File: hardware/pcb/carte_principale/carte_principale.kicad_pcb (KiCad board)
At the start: 2 copper layers, 54.5 x 50 mm, 20 parts, among them J1 Arduino_UNO_R3, J2 Conn_01x02, J3 Conn_01x02, P1 TE-FFC-10-0.5, P2 TE-FFC-10-0.5, U1 ESP-WROOM-02, U2 LSM6DS3, U3 BMP280, U4 74AHCT1G04, U5 74AHC1G125, U6 74LS166, U7 LIS2MDL

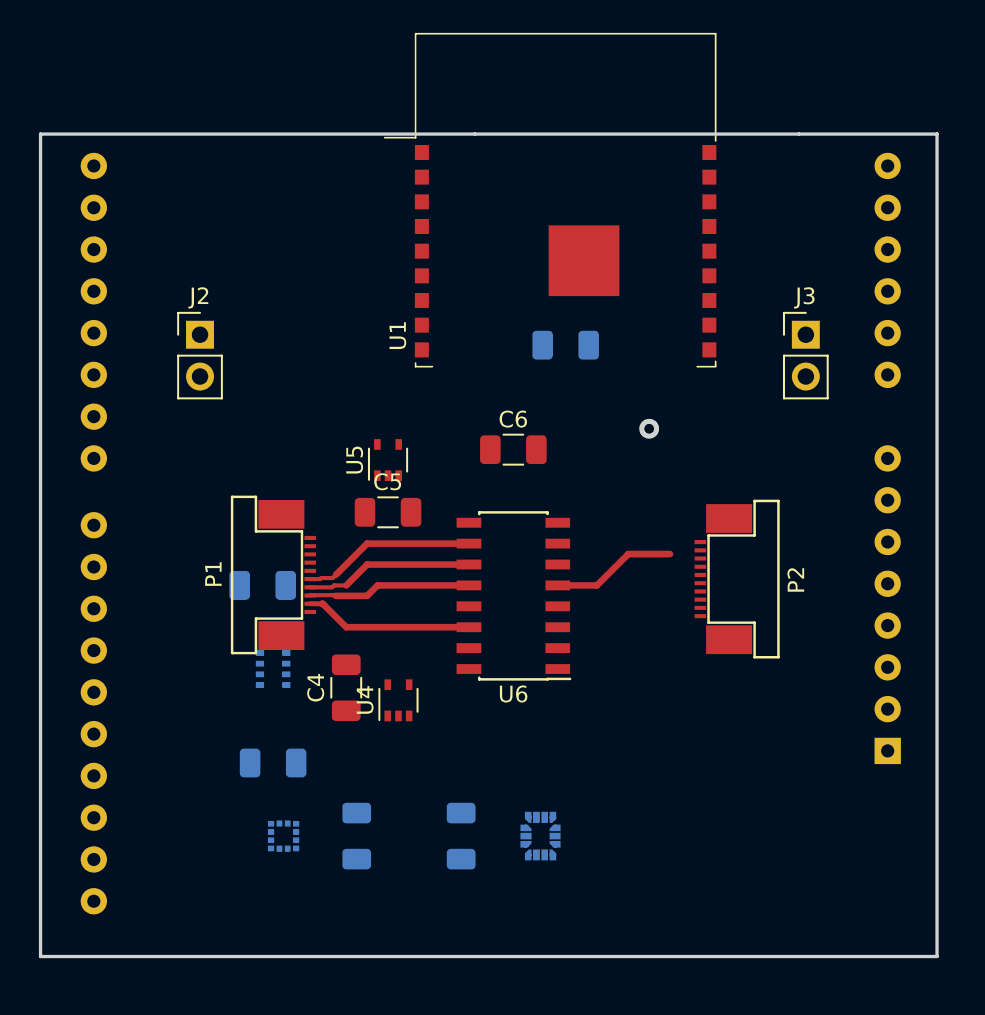
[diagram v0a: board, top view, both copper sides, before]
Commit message: ajout des pcb gauche et droit
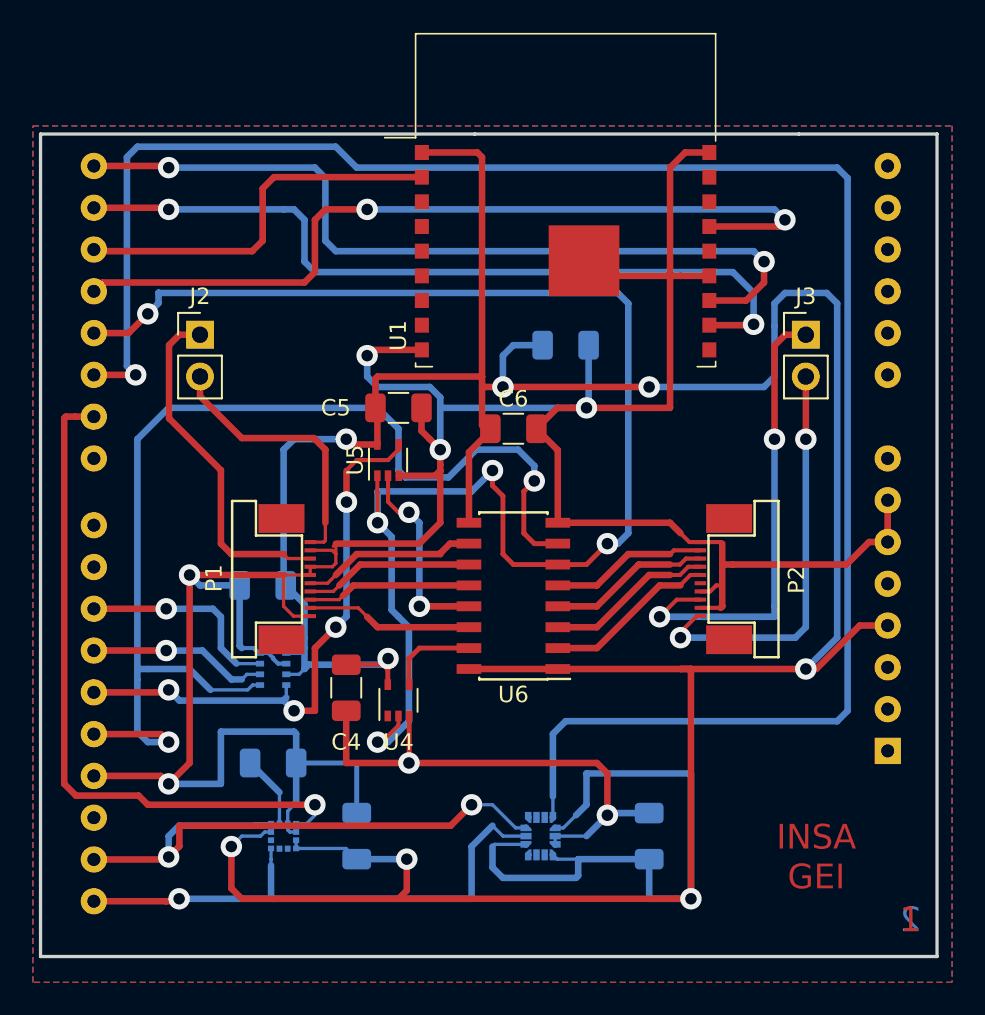
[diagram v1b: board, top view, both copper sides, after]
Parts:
- moved C2 11.4 mm to (127.0, 106.7)
- moved C5 6.38 mm to (111.8, 80.6)
- moved C6 1.27 mm to (118.7, 81.9)
- moved P1 0.25 mm to (106.0, 91.1)
- turned C4 to 270 degrees
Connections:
- C1 pad 1: VDD -> VCC
- C2 pad 1: VDD -> VCC
- C3 pad 1: VDD -> VCC
- C4 pad 1: VDD -> VCC
- C5 pad 1: VDD -> VCC
- C6 pad 1: VDD -> VCC
- C7 pad 1: VDD -> VCC
- J1 pad 4: VDD -> VCC
- U1 pad 1: VDD -> VCC
- U2 pad 12: VDD -> VCC
- U2 pad 5: VDD -> VCC
- U2 pad 8: VDD -> VCC
- U3 pad 6: VDD -> VCC
- U3 pad 8: VDD -> VCC
- U6 pad 1: VDD -> VCC
- U6 pad 16: VDD -> VCC
- U6 pad 9: VDD -> VCC
- U7 pad 10: VDD -> VCC
- U7 pad 3: VDD -> VCC
- U7 pad 9: VDD -> VCC
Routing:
- net VCC: track 0.00 -> 247.8 mm, vias 0 -> 8
- net GND: track 0.00 -> 217.6 mm, vias 0 -> 7
- net /IT_LSM6DS3: track 0.00 -> 116.8 mm, vias 0 -> 1
- net /KEYS_EN: track 0.00 -> 92.0 mm, vias 0 -> 5
- net /SPI_SCK: track 0.00 -> 68.8 mm, vias 0 -> 2
- net /WIFI_RST: track 0.00 -> 51.0 mm, vias 0 -> 2
- net /WIFI_TX: track 0.00 -> 50.4 mm, vias 0 -> 2
- net /WIFI_RX: track 0.00 -> 48.4 mm, vias 0 -> 2
- net /IT_LIS2MDL: track 0.00 -> 42.4 mm, vias 0 -> 1
- net /I2C_SDA: track 0.00 -> 36.8 mm, vias 0 -> 2
- net /SPI_MISO: track 0.00 -> 34.5 mm, vias 0 -> 4
- net /I2C_SCL: track 0.00 -> 33.4 mm, vias 0 -> 1
- net /Audio_Right_2: track 0.00 -> 28.6 mm, vias 0 -> 2
- net /Audio_Right_1: track 0.00 -> 25.1 mm, vias 0 -> 2
- net /WIFI_EN: track 0.00 -> 23.7 mm
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- added copper zone on B.Cu, net GND
- added copper zone on F.Cu, net GND
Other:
- board text added: "1"
- board text added: "2"
- board text added: "INSA GEI"

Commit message: ajout du wifi (debut) et mise a jour pcb
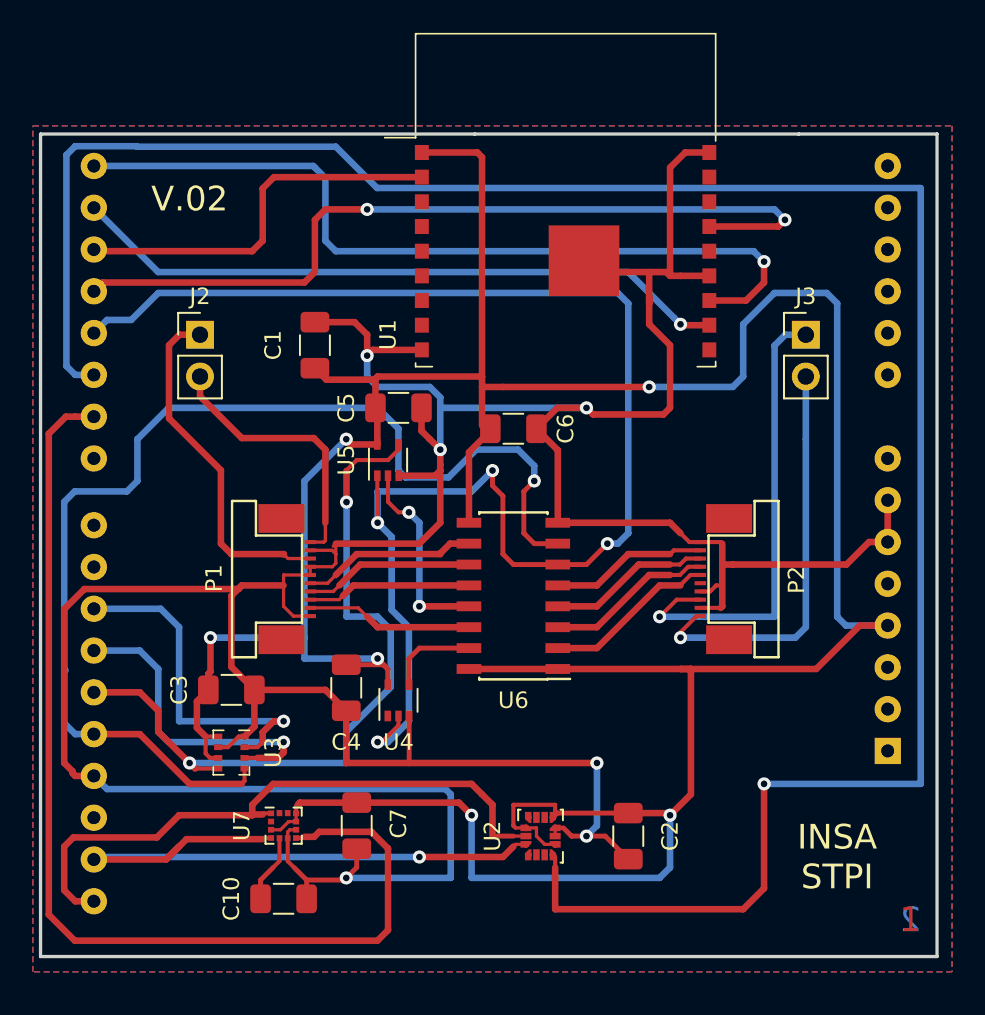
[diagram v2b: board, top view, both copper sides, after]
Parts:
- C1, C10, C2, C3, C7, U2, U3, U7: moved to F.Cu
- moved C1 15.2 mm to (106.7, 76.8), turned to 90 degrees
- moved C10 8.28 mm to (104.8, 110.5)
- moved C3 6.63 mm to (101.6, 97.8), turned to 0 degrees
- moved U3 5.68 mm to (101.6, 101.6)
- moved C2 1.27 mm to (125.7, 106.7), turned to 270 degrees
- moved C7 0.64 mm to (109.2, 106.0), turned to 270 degrees
- moved U7 0.64 mm to (104.8, 106.0)
- turned U2 to 90 degrees
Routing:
- net VCC: track 247.8 -> 214.6 mm, vias 8 -> 6
- net GND: track 217.6 -> 245.7 mm, vias 7 -> 6
- net /IT_LIS2MDL: track 42.4 -> 65.1 mm, vias 1 -> 0
- net /IT_LSM6DS3: track 116.8 -> 136.6 mm
- net /SPI_MISO: track 34.5 -> 44.9 mm, vias 4 -> 2
- net /EN_BMP280: track 12.6 -> 21.1 mm
- net /SPI_MOSI: track 11.0 -> 19.2 mm
- net /WIFI_RX: track 48.4 -> 40.4 mm, vias 2 -> 1
- net /I2C_SCL: track 33.4 -> 38.4 mm, vias 1 -> 0
- net /I2C_SDA: track 36.8 -> 38.9 mm, vias 2 -> 1
- net /SPI_SCK: track 68.8 -> 70.3 mm, vias 2 -> 1
- net /KEYS_EN: track 92.0 -> 91.6 mm, vias 5 -> 4
- net /WIFI_TX: vias 2 -> 1
- net /Audio_Right_2: vias 2 -> 1
- net /Audio_Right_1: vias 2 -> 1
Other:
- board text added: "INSA STPI"
- board text added: "V.02"
- board text removed: "INSA GEI"

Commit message: mise a jour des pcb et design mecaniques
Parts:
- added Logo1: LOGO, Insa:insa-image, F.Cu at (135.9, 110.4)
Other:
- board text added: "STPI"
- board text added: "V 02A"
- board text removed: "INSA STPI"
- board text removed: "V.02"

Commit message: Commit de sauvegarde
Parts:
- removed U4: 74AHCT1G04, Package_TO_SOT_SMD:SOT-353_SC-70-5
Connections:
- net /EN_BMP280 renamed /BMP280_EN
- net /IT_LIS2MDL renamed /LIS2MDL_IT
- net /IT_LSM6DS3 renamed /LSM6DS3_IT
- J1 pad 24: Net-(J1-Pad24) -> /KEYS_LOAD
- J1 pad 3: Net-(J1-Pad3) -> /KEY_RST
- P1 pad 7: GND -> VCC
- P2 pad 6: /Key_RST -> /KEY_RST
- P2 pad 7: GND -> VCC
- U6 pad 15: Net-(U4-Pad4) -> /KEYS_LOAD
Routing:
- net /KEYS_LOAD: track 0.00 -> 32.5 mm, vias 0 -> 1
- net /KEY_RST: track 0.00 -> 19.4 mm
- net VCC: track 214.6 -> 233.0 mm, vias 6 -> 7
- net /KEYS_EN: track 91.6 -> 74.0 mm, vias 4 -> 3
- net Net-(U4-Pad4): track 5.51 -> 0.00 mm
- net GND: track 245.7 -> 248.5 mm, vias 6 -> 8
- removed copper zone on B.Cu, net GND
- removed copper zone on F.Cu, net GND

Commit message: sauvegarde intermediaire
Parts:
- added R1: 10K, Resistor_SMD:R_1206_3216Metric, F.Cu at (117.9, 100.3)
- added R2: 10K, Resistor_SMD:R_1206_3216Metric, F.Cu at (115.6, 100.3)
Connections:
- U1 pad 6: Net-(U1-Pad6) -> GND
- U1 pad 8: Net-(U1-Pad8) -> VCC
- U2 pad 1: Net-(U2-Pad1) -> VCC
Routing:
- net VCC: track 233.0 -> 246.8 mm, vias 7 -> 9
- net /I2C_SDA: track 38.9 -> 45.5 mm, vias 1 -> 3
- net GND: track 248.5 -> 254.0 mm
- net /I2C_SCL: track 38.4 -> 40.4 mm
- added copper zone on B.Cu, net GND
- added copper zone on F.Cu, net GND
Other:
- board text added: "V 02B"
- board text removed: "V 02A"

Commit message: sauvegarde intermediaire
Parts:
- added JP1: SJ, Jumper:SolderJumper-2_P1.3mm_Open_RoundedPad1.0x1.5mm, F.Cu at (128.6, 111.1)
- added JP2: SJ, Jumper:SolderJumper-2_P1.3mm_Open_RoundedPad1.0x1.5mm, F.Cu at (126.7, 102.7)
- added JP3: SJ, Jumper:SolderJumper-2_P1.3mm_Open_RoundedPad1.0x1.5mm, F.Cu at (111.1, 110.8)
- U2: footprint Package_LGA:LGA-14_3x2.5mm_P0.5mm_LayoutBorder3x4y -> Insa:LGA-14_3x2.5mm_P0.5mm_LayoutBorder3x4y-slim
- U7: footprint Package_LGA:LGA-12_2x2mm_P0.5mm -> Insa:LGA-12_2x2mm_P0.5mm-slim
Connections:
- U2 pad 4: /LSM6DS3_IT -> Net-(JP1-Pad1)
- U7 pad 7: /LIS2MDL_IT -> Net-(JP3-Pad2)
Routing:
- net /LIS2MDL_IT: track 65.1 -> 54.9 mm
- net Net-(JP1-Pad1): track 0.00 -> 9.91 mm
- net Net-(JP3-Pad2): track 0.00 -> 8.89 mm
- net Net-(JP2-Pad1): track 0.00 -> 7.69 mm
- net VCC: track 246.8 -> 248.9 mm, vias 9 -> 11
- net /LSM6DS3_IT: track 136.6 -> 138.6 mm, vias 1 -> 2
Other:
- net class Default: clearance 0.2 -> 0.125
- net class Insa_GEI: clearance 0.2 -> 0.125
- net class Power: clearance 0.2 -> 0.125
- rule trace_clearance: 0.2 -> 0.125
- board text added: "V 02C"
- board text removed: "V 02B"
